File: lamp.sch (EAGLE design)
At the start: 54 parts

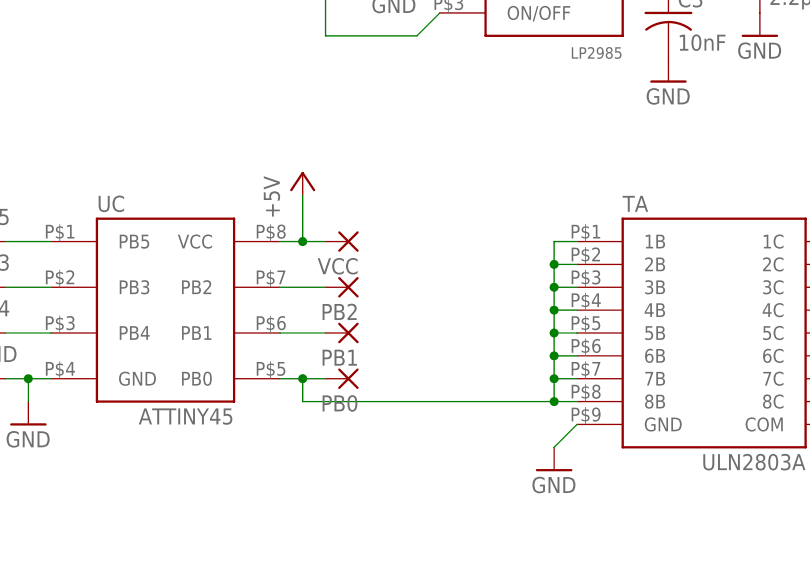
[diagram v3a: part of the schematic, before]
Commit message: More fiddling: moved some parts around, started adding capacitive touch on/off switch
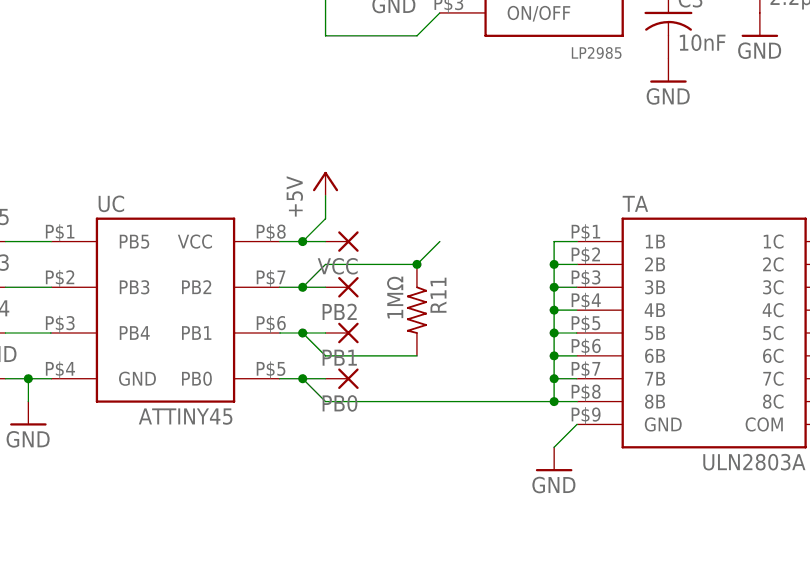
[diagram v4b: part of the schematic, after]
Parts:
- added R11: 1MΩ, Barebones-Arduino:RESISTOR-SMD
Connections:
- new net +5V: UC.VCC, VCC.P
- net N$14: now also R11.2
- net N$15: no longer UC.VCC, VCC.P
- net N$17: now also R11.1
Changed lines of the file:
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@@
 <part name="C3" library=" Barebones-Arduino" deviceset="CAPACITOR" device="-SMD" value="10nF"/>
 <part name="GND4" library=" Barebones-Arduino" deviceset="GND" device=""/>
+<part name="R11" library=" Barebones-Arduino" deviceset="RESISTOR" device="-SMD" value="1MΩ"/>
 </parts>
 <sheets>
@@
 <instance part="GND1" gate="1" x="45.72" y="25.4"/>
 <instance part="GND2" gate="1" x="-12.7" y="30.48"/>
-<instance part="P+2" gate="1" x="17.78" y="58.42"/>
+<instance part="P+2" gate="1" x="20.32" y="58.42"/>
 <instance part="GND3" gate="1" x="68.58" y="73.66"/>
 <instance part="P+3" gate="1" x="17.78" y="93.98"/>
@@
 <instance part="C3" gate="G$1" x="58.42" y="76.2"/>
 <instance part="GND4" gate="1" x="58.42" y="68.58"/>
+<instance part="R11" gate="G$1" x="30.48" y="43.18" rot="R270"/>
 </instances>
 <busses>
@@
 <wire x1="71.12" y1="83.82" x2="68.58" y2="83.82" width="0.1524" layer="91"/>
 </segment>
-<segment>
-<pinref part="UC" gate="G$1" pin="VCC"/>
-<pinref part="VCC" gate="1" pin="P"/>
-<wire x1="15.24" y1="50.8" x2="17.78" y2="50.8" width="0.1524" layer="91"/>
-<pinref part="P+2" gate="1" pin="+5V"/>
-<wire x1="17.78" y1="50.8" x2="20.32" y2="50.8" width="0.1524" layer="91"/>
-<wire x1="17.78" y1="55.88" x2="17.78" y2="50.8" width="0.1524" layer="91"/>
-<junction x="17.78" y="50.8"/>
-</segment>
 </net>
 <net name="N$14" class="0">
@@
 <pinref part="UC" gate="G$1" pin="PB1"/>
 <pinref part="PB1" gate="1" pin="P"/>
-<wire x1="15.24" y1="40.64" x2="20.32" y2="40.64" width="0.1524" layer="91"/>
+<wire x1="15.24" y1="40.64" x2="17.78" y2="40.64" width="0.1524" layer="91"/>
+<pinref part="R11" gate="G$1" pin="2"/>
+<wire x1="17.78" y1="40.64" x2="20.32" y2="40.64" width="0.1524" layer="91"/>
+<wire x1="17.78" y1="40.64" x2="20.32" y2="38.1" width="0.1524" layer="91"/>
+<wire x1="20.32" y1="38.1" x2="30.48" y2="38.1" width="0.1524" layer="91"/>
+<junction x="17.78" y="40.64"/>
 </segment>
 </net>
@@
 <pinref part="UC" gate="G$1" pin="PB2"/>
 <pinref part="PB2" gate="1" pin="P"/>
-<wire x1="15.24" y1="45.72" x2="20.32" y2="45.72" width="0.1524" layer="91"/>
+<wire x1="15.24" y1="45.72" x2="17.78" y2="45.72" width="0.1524" layer="91"/>
+<pinref part="R11" gate="G$1" pin="1"/>
+<wire x1="17.78" y1="45.72" x2="20.32" y2="45.72" width="0.1524" layer="91"/>
+<wire x1="17.78" y1="45.72" x2="20.32" y2="48.26" width="0.1524" layer="91"/>
+<wire x1="20.32" y1="48.26" x2="30.48" y2="48.26" width="0.1524" layer="91"/>
+<junction x="17.78" y="45.72"/>
+<wire x1="30.48" y1="48.26" x2="33.02" y2="50.8" width="0.1524" layer="91"/>
+<junction x="30.48" y="48.26"/>
 </segment>
 </net>
@@
 <wire x1="15.24" y1="35.56" x2="17.78" y2="35.56" width="0.1524" layer="91"/>
 <wire x1="17.78" y1="35.56" x2="20.32" y2="35.56" width="0.1524" layer="91"/>
-<wire x1="17.78" y1="35.56" x2="17.78" y2="33.02" width="0.1524" layer="91"/>
+<wire x1="17.78" y1="35.56" x2="20.32" y2="33.02" width="0.1524" layer="91"/>
 <junction x="17.78" y="35.56"/>
 <pinref part="TA" gate="G$1" pin="1B"/>
@@
 <wire x1="48.26" y1="33.02" x2="45.72" y2="33.02" width="0.1524" layer="91"/>
 <wire x1="45.72" y1="33.02" x2="45.72" y2="35.56" width="0.1524" layer="91"/>
-<wire x1="17.78" y1="33.02" x2="45.72" y2="33.02" width="0.1524" layer="91"/>
+<wire x1="20.32" y1="33.02" x2="45.72" y2="33.02" width="0.1524" layer="91"/>
 <junction x="45.72" y="33.02"/>
 </segment>
@@
 </segment>
 </net>
+<net name="+5V" class="0">
+<segment>
+<pinref part="UC" gate="G$1" pin="VCC"/>
+<pinref part="VCC" gate="1" pin="P"/>
+<wire x1="15.24" y1="50.8" x2="17.78" y2="50.8" width="0.1524" layer="91"/>
+<pinref part="P+2" gate="1" pin="+5V"/>
+<wire x1="17.78" y1="50.8" x2="20.32" y2="50.8" width="0.1524" layer="91"/>
+<wire x1="17.78" y1="50.8" x2="20.32" y2="53.34" width="0.1524" layer="91"/>
+<wire x1="20.32" y1="53.34" x2="20.32" y2="55.88" width="0.1524" layer="91"/>
+<junction x="17.78" y="50.8"/>
+</segment>
+</net>

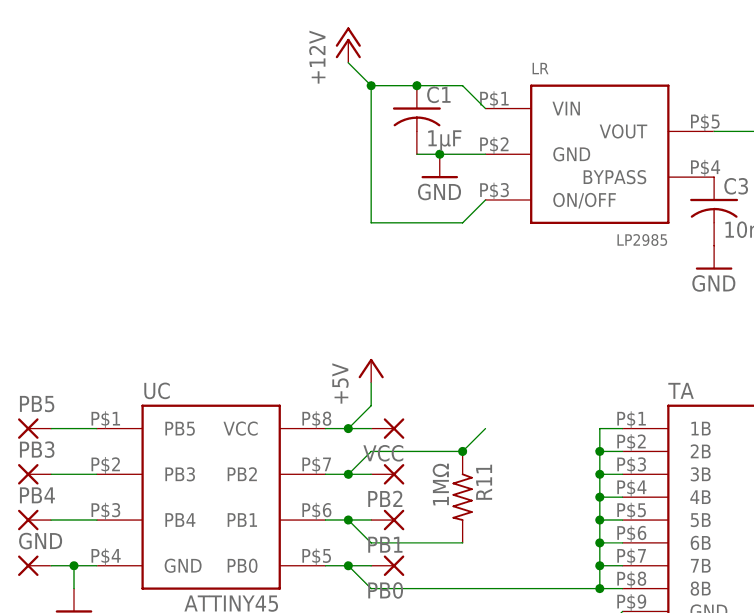
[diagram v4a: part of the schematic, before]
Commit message: Fixed some footprints, mangled some others, and added a temporary placeholder for the header block that will be for power and the switch.
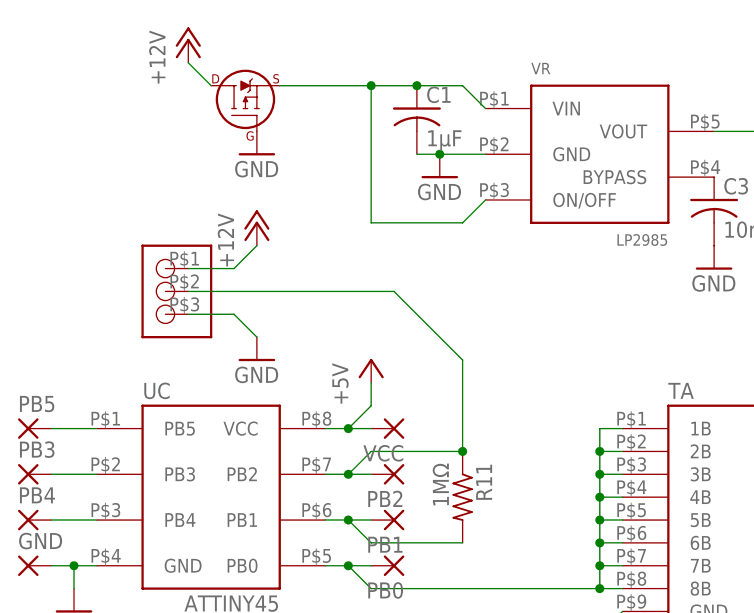
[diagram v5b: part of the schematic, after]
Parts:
- added U$19: SI2319DS, lamp:SI2319DS
- added U$32: HEADER-3X1, lamp:HEADER-3X1
- renumbered LR to VR
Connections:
- new net N$45: C1.1, U$19.SOURCE, VR.ON/OFF, VR.VIN
- net +12V: now also U$19.DRAIN, U$32.P$1; no longer C1.1, VR.ON/OFF, VR.VIN
- net GND: now also U$19.GATE, U$32.P$3
- net N$17: now also U$32.P$2
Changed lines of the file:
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@@
 <part name="P+3" library=" Barebones-Arduino" deviceset="+12V" device=""/>
 <part name="GND5" library=" Barebones-Arduino" deviceset="GND" device=""/>
-<part name="LR" library="lamp" deviceset="LP2985" device=""/>
+<part name="VR" library="lamp" deviceset="LP2985" device=""/>
 <part name="C1" library=" Barebones-Arduino" deviceset="CAPACITOR" device="-SMD" value="1µF"/>
 <part name="C2" library=" Barebones-Arduino" deviceset="CAPACITOR" device="-SMD" value="2.2µF"/>
@@
 <part name="GND4" library=" Barebones-Arduino" deviceset="GND" device=""/>
 <part name="R11" library=" Barebones-Arduino" deviceset="RESISTOR" device="-SMD" value="1MΩ"/>
+<part name="U$19" library="lamp" deviceset="SI2319DS" device=""/>
+<part name="GND6" library=" Barebones-Arduino" deviceset="GND" device=""/>
+<part name="U$32" library="lamp" deviceset="HEADER-3X1" device=""/>
+<part name="P+5" library=" Barebones-Arduino" deviceset="+12V" device=""/>
+<part name="GND7" library=" Barebones-Arduino" deviceset="GND" device=""/>
 </parts>
 <sheets>
@@
 <instance part="P+2" gate="1" x="20.32" y="58.42"/>
 <instance part="GND3" gate="1" x="68.58" y="73.66"/>
-<instance part="P+3" gate="1" x="17.78" y="93.98"/>
+<instance part="P+3" gate="1" x="0" y="93.98"/>
 <instance part="GND5" gate="1" x="27.94" y="78.74"/>
-<instance part="LR" gate="G$1" x="45.72" y="81.28"/>
+<instance part="VR" gate="G$1" x="45.72" y="81.28"/>
 <instance part="C1" gate="G$1" x="25.4" y="86.36"/>
 <instance part="C2" gate="G$1" x="68.58" y="81.28"/>
@@
 <instance part="GND4" gate="1" x="58.42" y="68.58"/>
 <instance part="R11" gate="G$1" x="30.48" y="43.18" rot="R270"/>
+<instance part="U$19" gate="G$1" x="5.08" y="88.9"/>
+<instance part="GND6" gate="1" x="7.62" y="81.28"/>
+<instance part="U$32" gate="G$1" x="0" y="68.58"/>
+<instance part="P+5" gate="1" x="7.62" y="73.66"/>
+<instance part="GND7" gate="1" x="7.62" y="58.42"/>
 </instances>
 <busses>
@@
 </segment>
 <segment>
-<pinref part="C1" gate="G$1" pin="1"/>
-<pinref part="LR" gate="G$1" pin="ON/OFF"/>
-<wire x1="33.02" y1="76.2" x2="30.48" y2="73.66" width="0.1524" layer="91"/>
-<wire x1="30.48" y1="73.66" x2="20.32" y2="73.66" width="0.1524" layer="91"/>
-<wire x1="20.32" y1="73.66" x2="20.32" y2="88.9" width="0.1524" layer="91"/>
-<wire x1="20.32" y1="88.9" x2="25.4" y2="88.9" width="0.1524" layer="91"/>
-<wire x1="25.4" y1="88.9" x2="30.48" y2="88.9" width="0.1524" layer="91"/>
-<junction x="25.4" y="88.9"/>
-<pinref part="LR" gate="G$1" pin="VIN"/>
-<wire x1="30.48" y1="88.9" x2="33.02" y2="86.36" width="0.1524" layer="91"/>
 <pinref part="P+3" gate="1" pin="+12V"/>
-<wire x1="17.78" y1="91.44" x2="20.32" y2="88.9" width="0.1524" layer="91"/>
-<junction x="20.32" y="88.9"/>
+<pinref part="U$19" gate="G$1" pin="DRAIN"/>
+<wire x1="0" y1="91.44" x2="2.54" y2="88.9" width="0.1524" layer="91"/>
+</segment>
+<segment>
+<pinref part="U$32" gate="G$1" pin="P$1"/>
+<wire x1="0" y1="68.58" x2="5.08" y2="68.58" width="0.1524" layer="91"/>
+<wire x1="5.08" y1="68.58" x2="7.62" y2="71.12" width="0.1524" layer="91"/>
+<pinref part="P+5" gate="1" pin="+12V"/>
 </segment>
 </net>
@@
 <pinref part="GND5" gate="1" pin="GND"/>
 <junction x="27.94" y="81.28"/>
-<pinref part="LR" gate="G$1" pin="GND"/>
+<pinref part="VR" gate="G$1" pin="GND"/>
 <wire x1="27.94" y1="81.28" x2="33.02" y2="81.28" width="0.1524" layer="91"/>
 <wire x1="27.94" y1="81.28" x2="25.4" y2="81.28" width="0.1524" layer="91"/>
@@
 <pinref part="GND4" gate="1" pin="GND"/>
 </segment>
+<segment>
+<pinref part="U$19" gate="G$1" pin="GATE"/>
+<pinref part="GND6" gate="1" pin="GND"/>
+</segment>
+<segment>
+<pinref part="U$32" gate="G$1" pin="P$3"/>
+<wire x1="0" y1="63.5" x2="5.08" y2="63.5" width="0.1524" layer="91"/>
+<wire x1="7.62" y1="60.96" x2="5.08" y2="63.5" width="0.1524" layer="91"/>
+<pinref part="GND7" gate="1" pin="GND"/>
+</segment>
 </net>
 <net name="N$15" class="0">
@@
 <pinref part="P+4" gate="1" pin="+5V"/>
 <wire x1="73.66" y1="86.36" x2="71.12" y2="83.82" width="0.1524" layer="91"/>
-<pinref part="LR" gate="G$1" pin="VOUT"/>
+<pinref part="VR" gate="G$1" pin="VOUT"/>
 <pinref part="C2" gate="G$1" pin="1"/>
 <wire x1="58.42" y1="83.82" x2="68.58" y2="83.82" width="0.1524" layer="91"/>
@@
 <wire x1="20.32" y1="48.26" x2="30.48" y2="48.26" width="0.1524" layer="91"/>
 <junction x="17.78" y="45.72"/>
-<wire x1="30.48" y1="48.26" x2="33.02" y2="50.8" width="0.1524" layer="91"/>
 <junction x="30.48" y="48.26"/>
+<pinref part="U$32" gate="G$1" pin="P$2"/>
+<wire x1="0" y1="66.04" x2="22.86" y2="66.04" width="0.1524" layer="91"/>
+<wire x1="22.86" y1="66.04" x2="30.48" y2="58.42" width="0.1524" layer="91"/>
+<wire x1="30.48" y1="58.42" x2="30.48" y2="48.26" width="0.1524" layer="91"/>
 </segment>
 </net>
@@
 <net name="N$46" class="0">
 <segment>
-<pinref part="LR" gate="G$1" pin="BYPASS"/>
+<pinref part="VR" gate="G$1" pin="BYPASS"/>
 <pinref part="C3" gate="G$1" pin="1"/>
 </segment>
@@
 </segment>
 </net>
+<net name="N$45" class="0">
+<segment>
+<pinref part="C1" gate="G$1" pin="1"/>
+<pinref part="VR" gate="G$1" pin="ON/OFF"/>
+<wire x1="33.02" y1="76.2" x2="30.48" y2="73.66" width="0.1524" layer="91"/>
+<wire x1="30.48" y1="73.66" x2="20.32" y2="73.66" width="0.1524" layer="91"/>
+<wire x1="20.32" y1="73.66" x2="20.32" y2="88.9" width="0.1524" layer="91"/>
+<wire x1="20.32" y1="88.9" x2="25.4" y2="88.9" width="0.1524" layer="91"/>
+<wire x1="25.4" y1="88.9" x2="30.48" y2="88.9" width="0.1524" layer="91"/>
+<junction x="25.4" y="88.9"/>
+<pinref part="VR" gate="G$1" pin="VIN"/>
+<wire x1="30.48" y1="88.9" x2="33.02" y2="86.36" width="0.1524" layer="91"/>
+<pinref part="U$19" gate="G$1" pin="SOURCE"/>
+<wire x1="10.16" y1="88.9" x2="20.32" y2="88.9" width="0.1524" layer="91"/>
+<junction x="20.32" y="88.9"/>
+</segment>
+</net>

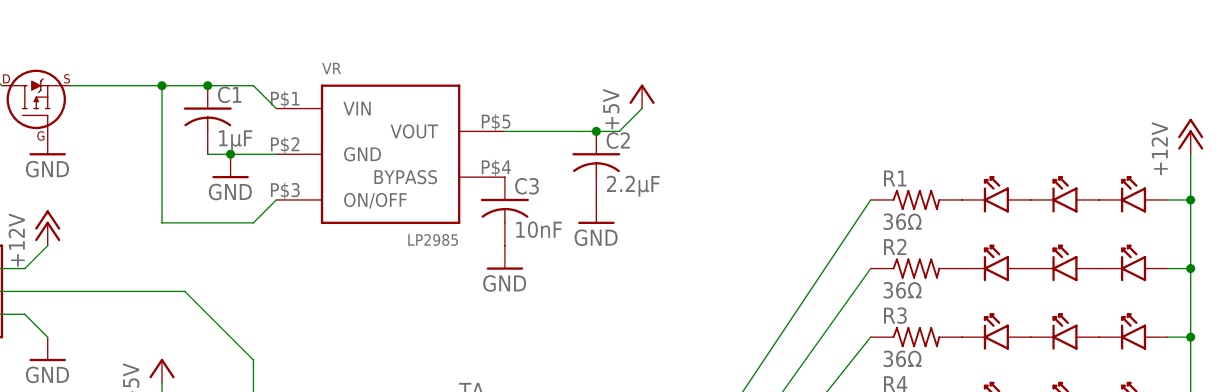
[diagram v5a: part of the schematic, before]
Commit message: fixed led vsupply to be from the pfet added in last commit instead of straight from +12v
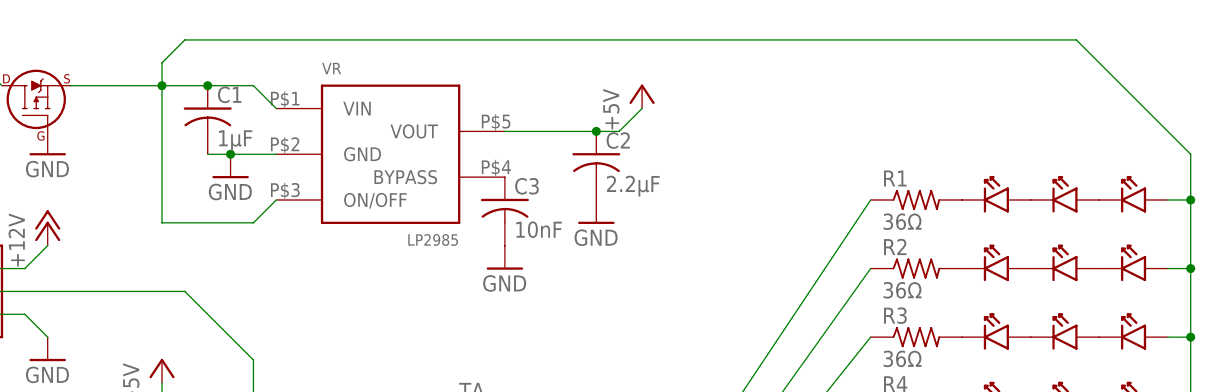
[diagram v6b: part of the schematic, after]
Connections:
- net +12V: no longer TA.COM, U$1.P$2, U$11.P$2, U$16.P$2, U$2.P$2, U$20.P$2, U$23.P$2, U$26.P$2, U$29.P$2, U$5.P$2, U$8.P$2
- net N$45: now also TA.COM, U$1.P$2, U$11.P$2, U$16.P$2, U$2.P$2, U$20.P$2, U$23.P$2, U$26.P$2, U$29.P$2, U$5.P$2, U$8.P$2
